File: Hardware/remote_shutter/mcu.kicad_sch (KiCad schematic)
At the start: 17 parts

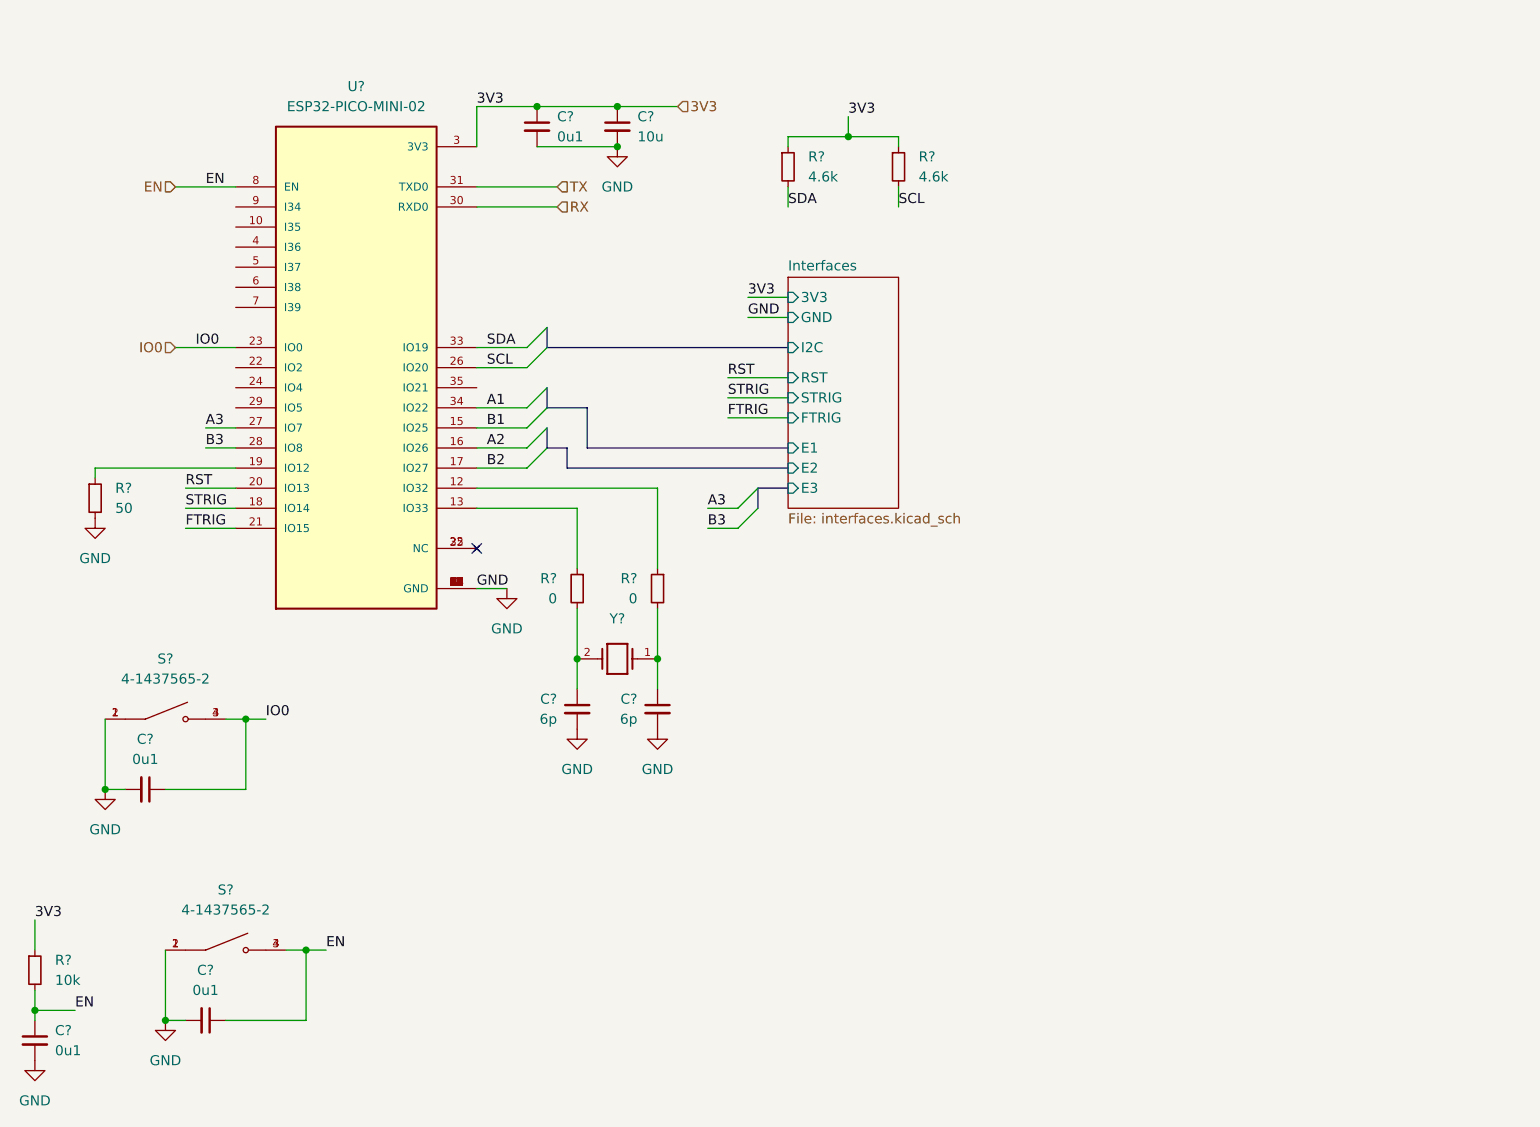
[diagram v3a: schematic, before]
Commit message: Added missing footprints. First PCB export.
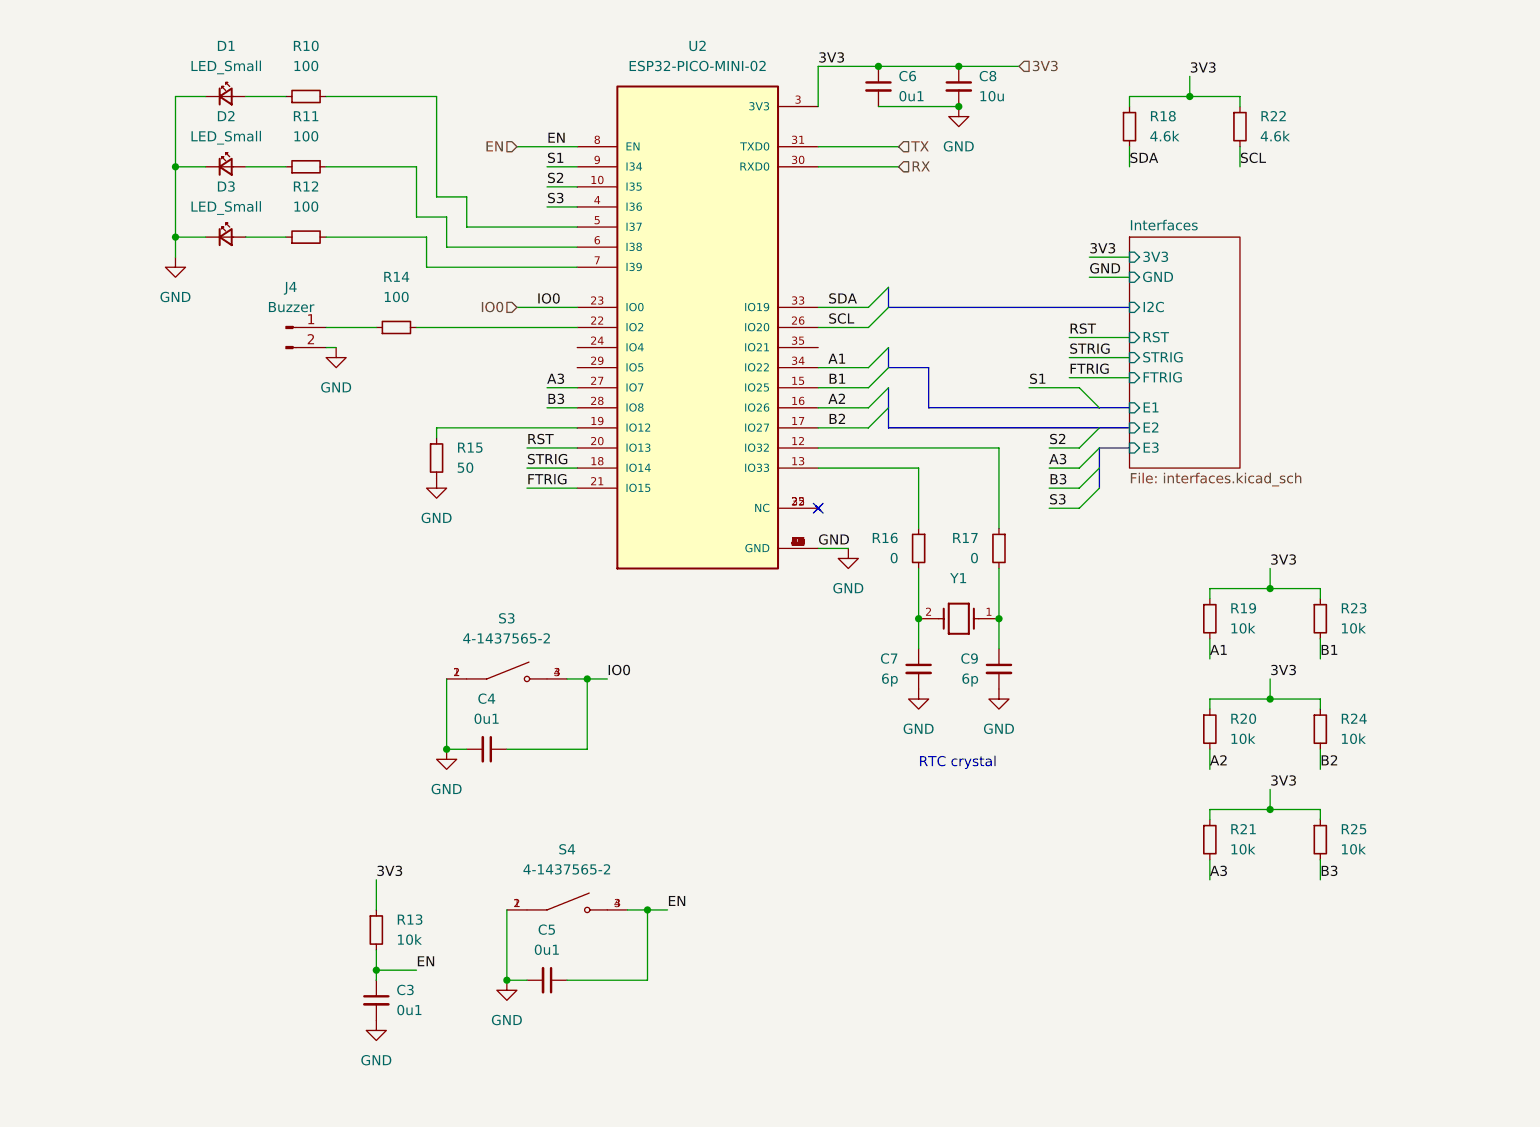
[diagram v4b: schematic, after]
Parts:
- added D1, D2, D3: LED_Small, LED_SMD:LED_0603_1608Metric_Pad1.05x0.95mm_HandSolder, symbol Device:LED_Small
- added J4: Buzzer, Connector_PinSocket_2.54mm:PinSocket_1x02_P2.54mm_Vertical, symbol Connector:Conn_01x02_Male
- added R10, R11, R12, R14: 100, Resistor_SMD:R_0603_1608Metric_Pad0.98x0.95mm_HandSolder, symbol Device:R_Small
- added R19, R20, R21, R23, R24, R25: 10k, Resistor_SMD:R_0603_1608Metric_Pad0.98x0.95mm_HandSolder, symbol Device:R_Small
- C3, C4, C6: renamed from C?; footprint (none) -> Capacitor_SMD:C_0603_1608Metric_Pad1.08x0.95mm_HandSolder
- C8: renamed from C?; footprint (none) -> Capacitor_SMD:C_0805_2012Metric_Pad1.18x1.45mm_HandSolder
- S3, S4: renamed from S?; footprint SW_4-1437565-2 -> footprint:SW_4-1437565-2
- U2: renamed from U?; footprint MODULE_ESP32-PICO-MINI-02 -> footprint:MODULE_ESP32-PICO-MINI-02
- Y1: renamed from Y?; footprint XTAL_NX3215SA-32.768K-STD-MUA-14 -> footprint:XTAL_NX3215SA-32.768K-STD-MUA-14
- gave numbers to parts that had none: 9
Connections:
- net 3V3: now also R19.1, R20.1, R21.1, R23.1, R24.1, R25.1
- net A1: now also R19.2
- net A2: now also R20.2
- net A3: now also R21.2
- net B1: now also R23.2
- net B2: now also R24.2
- net B3: now also R25.2
- net GND: now also D1.1 (K), D2.1 (K), D3.1 (K), J4.2 (Pin_2)
- net S2: now reaches U2.10 (I35)
- net at U2.22 (IO2): now also R14.2
- net S3: now reaches U2.4 (I36)
- net at U2.5 (I37): now also R10.2
- net at U2.6 (I38): now also R11.2
- net at U2.7 (I39): now also R12.2
- net S1: now reaches U2.9 (I34)
- new net: D2.2 (A), R11.1
- new net: D3.2 (A), R12.1
- new net: J4.1 (Pin_1), R14.1
- new net: D1.2 (A), R10.1
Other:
- note added: "RTC crystal"
- moved on the sheet: C3, C4, C5, C6, C7, C8, C9, R13, R15, R16, R17, R18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

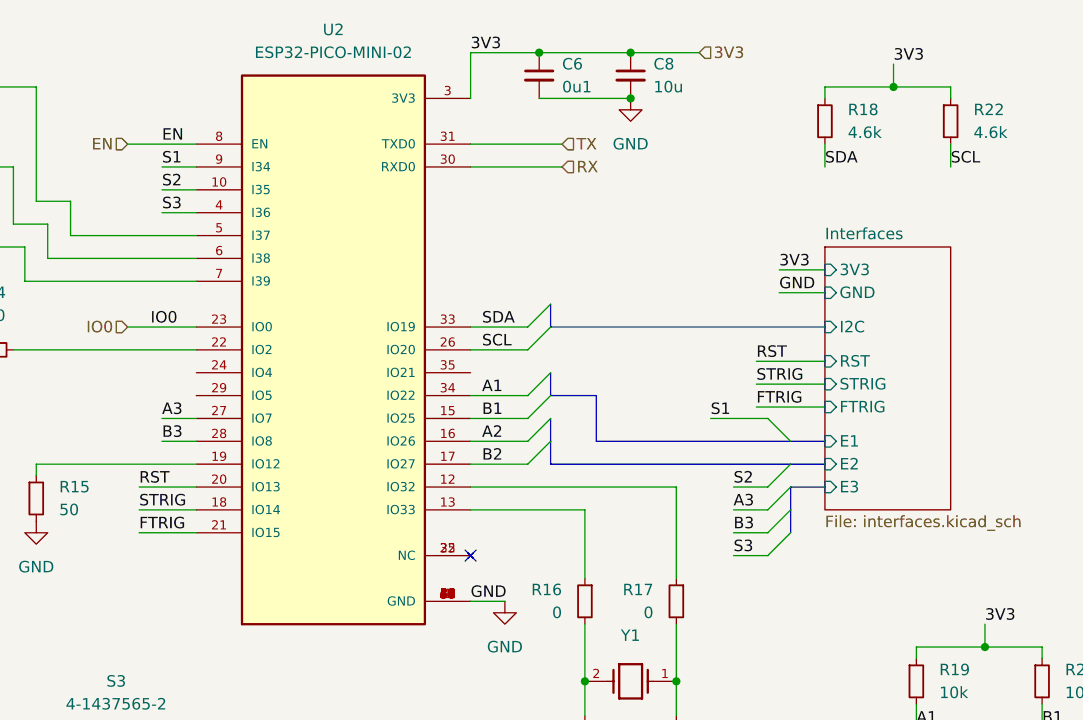
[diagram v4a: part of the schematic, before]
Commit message: Fixed bus routing
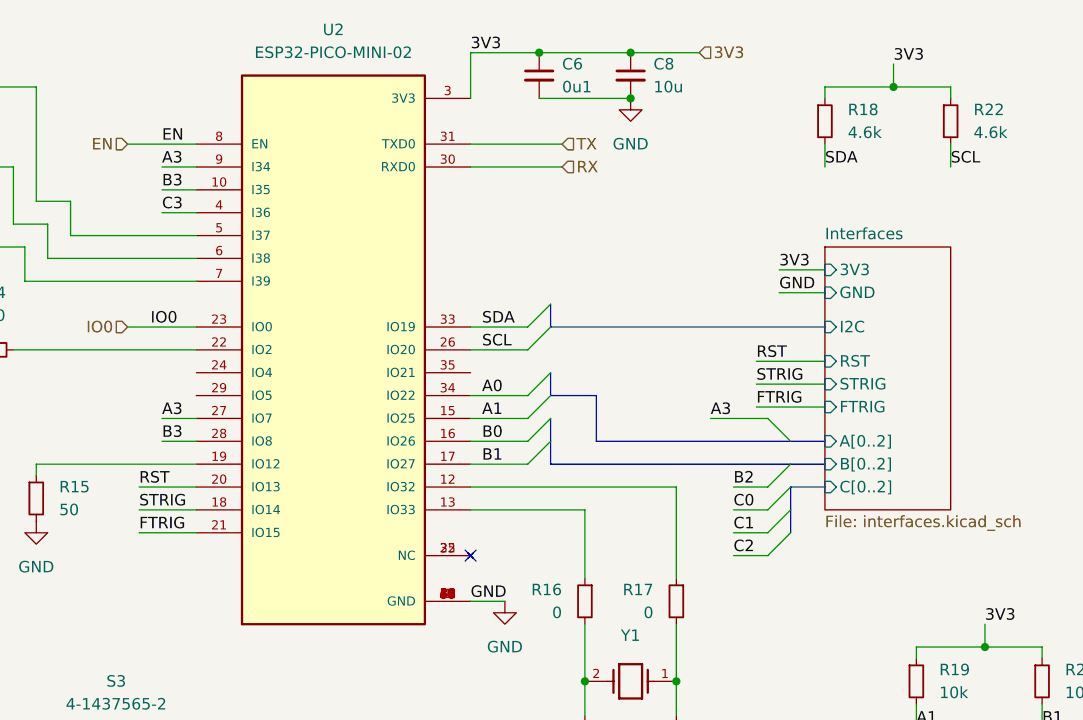
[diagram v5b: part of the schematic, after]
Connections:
- net S1 is gone; now on net A3: U2.9 (I34)
- net S2 is gone; now on net B3: U2.10 (I35)
- net A1: now also U2.15 (IO25); no longer U2.34 (IO22)
- net A2: no longer U2.16 (IO26)
- net B1: now also U2.17 (IO27); no longer U2.15 (IO25)
- net B2: no longer U2.17 (IO27)
- net S3 renamed C3
- new net A0: U2.34 (IO22)
- new net B0: U2.16 (IO26)
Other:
- sheet Interfaces ports: added A[0..2], B[0..2], C[0..2]; removed E1, E2, E3
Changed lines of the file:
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@@
     (effects (font (size 1.27 1.27)) (justify left bottom))
   )
-  (label "A1" (at 152.4 83.82 0)
+  (label "A0" (at 152.4 83.82 0)
     (effects (font (size 1.27 1.27)) (justify left bottom))
   )
@@
     (effects (font (size 1.27 1.27)) (justify left bottom))
   )
-  (label "S2" (at 180.34 93.98 0)
-    (effects (font (size 1.27 1.27)) (justify left bottom))
-  )
-  (label "B2" (at 152.4 91.44 0)
+  (label "B2" (at 180.34 93.98 0)
+    (effects (font (size 1.27 1.27)) (justify left bottom))
+  )
+  (label "B1" (at 152.4 91.44 0)
     (effects (font (size 1.27 1.27)) (justify left bottom))
   )
@@
     (effects (font (size 1.27 1.27)) (justify left bottom))
   )
-  (label "B3" (at 180.34 99.06 0)
+  (label "C1" (at 180.34 99.06 0)
     (effects (font (size 1.27 1.27)) (justify left bottom))
   )
@@
     (effects (font (size 1.27 1.27)) (justify left bottom))
   )
-  (label "S3" (at 116.84 63.5 0)
+  (label "C3" (at 116.84 63.5 0)
     (effects (font (size 1.27 1.27)) (justify left bottom))
   )
@@
     (effects (font (size 1.27 1.27)) (justify left bottom))
   )
-  (label "S1" (at 177.8 86.36 0)
+  (label "A3" (at 177.8 86.36 0)
     (effects (font (size 1.27 1.27)) (justify left bottom))
   )
@@
     (effects (font (size 1.27 1.27)) (justify left bottom))
   )
-  (label "B1" (at 152.4 86.36 0)
+  (label "A1" (at 152.4 86.36 0)
     (effects (font (size 1.27 1.27)) (justify left bottom))
   )
@@
     (effects (font (size 1.27 1.27)) (justify left bottom))
   )
-  (label "S3" (at 180.34 101.6 0)
+  (label "C2" (at 180.34 101.6 0)
     (effects (font (size 1.27 1.27)) (justify left bottom))
   )
@@
     (effects (font (size 1.27 1.27)) (justify left bottom))
   )
-  (label "S1" (at 116.84 58.42 0)
-    (effects (font (size 1.27 1.27)) (justify left bottom))
-  )
-  (label "S2" (at 116.84 60.96 0)
-    (effects (font (size 1.27 1.27)) (justify left bottom))
-  )
-  (label "A2" (at 152.4 88.9 0)
+  (label "A3" (at 116.84 58.42 0)
+    (effects (font (size 1.27 1.27)) (justify left bottom))
+  )
+  (label "B3" (at 116.84 60.96 0)
+    (effects (font (size 1.27 1.27)) (justify left bottom))
+  )
+  (label "B0" (at 152.4 88.9 0)
     (effects (font (size 1.27 1.27)) (justify left bottom))
   )
@@
     (effects (font (size 1.27 1.27)) (justify left bottom))
   )
-  (label "A3" (at 180.34 96.52 0)
+  (label "C0" (at 180.34 96.52 0)
     (effects (font (size 1.27 1.27)) (justify left bottom))
   )
@@
       (effects (font (size 1.27 1.27)) (justify left))
     )
-    (pin "E1" input (at 190.5 88.9 180)
-      (effects (font (size 1.27 1.27)) (justify left))
-    )
-    (pin "E2" input (at 190.5 91.44 180)
+    (pin "A[0..2]" input (at 190.5 88.9 180)
+      (effects (font (size 1.27 1.27)) (justify left))
+    )
+    (pin "B[0..2]" input (at 190.5 91.44 180)
       (effects (font (size 1.27 1.27)) (justify left))
     )
@@
       (effects (font (size 1.27 1.27)) (justify left))
     )
-    (pin "E3" input (at 190.5 93.98 180)
-      (effects (font (size 1.27 1.27)) (justify left))
-    )
+    (pin "C[0..2]" input (at 190.5 93.98 180)
+      (effects (font (size 1.27 1.27)) (justify left))
+    )
